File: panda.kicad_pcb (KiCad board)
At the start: 2 copper layers, 100 x 125 mm, 196 parts, among them J1 PIN10-13_Breakout, J10 24V_Lockout_Key_Switch, J11 XT60-M, J12 PT_1, J13 PT_4, J14 PT_2, J15 PT_5, J16 PT_3, J17 PT_6, J18 4-Pin Load Cell, J19 5-Pin Load Cell, J2 PIN6-9_Breakout, J20 Ignitor Screw Terminal, J21 Screw_Terminal_01x03, J22 Screw_Terminal_01x02, J3 USB_C_Receptacle_USB2.0_16P, J4 Valve_1_PWR, J5 Valve_4_PWR, J6 Valve_2_PWR, J7 Valve_5_PWR, J8 Valve_3_PWR, J9 Valve_6_PWR, K1 G5Q-1A DC24, K2 G5Q-1A DC24, Q1 BSS138, Q2 BSS138, Q3 BSS138, Q4 BSS138, Q5 BSS138, Q6 BSS138, Q7 BSS138, Q8 BSS138, SW1 PTS636SM43SMTR LFS, SW2 PTS636SM43SMTR LFS, U1 ESP32-S3-WROOM-1, U2 ADS112C04, U3 ADS112C04, U4 ADS112C04, U5 ADS112C04, U6 TPS5430DDA, U7 XC6220B331PR-G, U8 INA199A2DCK

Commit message: pcb first draft, changed esp32 pin connections
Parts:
- removed the C15 at (263.8, 51.6)
- removed the C15 at (249.8, 59.5)
- removed the C5 at (205.4, 99.3)
- removed the C5 at (211.0, 71.5)
- removed J2: PIN6-9_Breakout, TerminalBlock:TerminalBlock_Xinya_XY308-2.54-4P_1x04_P2.54mm_Horizontal
- removed the R2 at (202.0, 90.8)
- added C15: 10uF, Capacitor_SMD:C_1206_3216Metric, F.Cu at (122.2, 70.7)
- added C22: 0.1uF, Capacitor_SMD:C_0603_1608Metric, F.Cu at (131.1, 36.6)
- added C23: 0.1uF, Capacitor_SMD:C_0603_1608Metric, F.Cu at (131.1, 30.0)
- added C5: 0.1uF, Capacitor_SMD:C_0402_1005Metric, F.Cu at (153.1, 36.1)
- added D17: TSD24DYFR, Diode_SMD:D_SOD-323, F.Cu at (129.3, 36.6)
- added D18: TSD24DYFR, Diode_SMD:D_SOD-323, F.Cu at (129.3, 29.9)
- added R47: 10, Resistor_SMD:R_0402_1005Metric, F.Cu at (127.5, 34.3)
- added R48: 10, Resistor_SMD:R_0402_1005Metric, F.Cu at (127.5, 32.0)
- moved C19 164.5 mm to (119.0, 82.4)
- moved D12 152.4 mm to (118.2, 69.4)
- moved R37 150.1 mm to (130.1, 61.3), turned to 90 degrees
- moved D13 149.0 mm to (122.2, 68.2), turned to 0 degrees
- moved U7 140.4 mm to (120.2, 75.5), turned to -90 degrees
- moved C17 133.8 mm to (120.0, 80.4)
- moved D15 127.3 mm to (127.7, 61.3)
- moved R36 113.0 mm to (125.2, 68.2), turned to -90 degrees
- moved TP4 112.8 mm to (117.2, 84.2), turned to 180 degrees
- moved G*** 94.1 mm to (134.4, 95.1)
- moved R7 84.1 mm to (155.7, 64.5)
- moved R8 84.0 mm to (155.7, 65.8)
- moved C2 79.6 mm to (156.5, 57.7), turned to 180 degrees
- moved J1 77.9 mm to (165.4, 105.7)
- moved D8 76.0 mm to (127.7, 52.5)
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- renumbered C22 to C24, C23 to C25, C24 to C26, C25 to C27, C26 to C28, C27 to C29, C28 to C30, C29 to C31, C30 to C32, C31 to C33, C32 to C34, C33 to C35, C34 to C36, C35 to C37, C36 to C38, C37 to C39, D8 to D10, D10 to D11, D11 to D12, D12 to D13, D13 to D14, D14 to D15, D15 to D16, D16 to D19, D17 to D20, D18 to D21, D19 to D22, D20 to D23, D21 to D24, D22 to D25, D23 to D26, D24 to D27, D25 to D28, D26 to D29, D27 to D30, D28 to D31, D29 to D32, D30 to D33, D31 to D34, D32 to D35, D33 to D36, D34 to D8, J11 to J10, J10 to J11, R11 to R10, R12 to R11, R13 to R12, R14 to R13, R15 to R14, R16 to R15, R17 to R16, R18 to R17, R19 to R18, R20 to R19, R3 to R2, R21 to R20, R22 to R21, R23 to R22, R24 to R23, R25 to R24, R26 to R25, R27 to R26, R28 to R27, R29 to R28, R68 to R29, R4 to R3, R33 to R32, R32 to R33, R5 to R4, R47 to R49, R6 to R5, R48 to R50, R49 to R51, R50 to R52, R51 to R53, R52 to R54, R53 to R55, R54 to R56, R55 to R57, R56 to R58, R57 to R59, R7 to R6, R58 to R60, R59 to R61, R60 to R62, R61 to R63, R62 to R64, R63 to R65, R64 to R66, R65 to R67, R66 to R68, R67 to R69, R8 to R7, R9 to R8, R10 to R9
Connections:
- F1 pad 2: Net-(U8-+) -> Net-(F1-Pad2)
- J1 pad 1: unconnected-(J1-Pin_1-Pad1) -> MTMS
- J1 pad 2: unconnected-(J1-Pin_2-Pad2) -> MTDI
- J1 pad 3: unconnected-(J1-Pin_3-Pad3) -> MTDO
- J1 pad 4: unconnected-(J1-Pin_4-Pad4) -> MTCK
- J3 pad S1: Net-(J3-SHIELD) -> unconnected-(J3-SHIELD-PadS1)
- R49 pad 1: Net-(U8-+) -> Net-(F1-Pad2)
- U1 pad 10: VALVE_4_CTL -> VALVE_5_CTL
- U1 pad 11: VALVE_5_CTL -> VALVE_4_CTL
- U1 pad 12: VALVE_6_CTL -> VALVE_3_CTL
- U1 pad 15: I2C_SCL -> I2C_SDA
- U1 pad 16: I2C_SDA -> I2C_SCL
- U1 pad 32: unconnected-(U1-IO39-Pad32) -> MTCK
- U1 pad 33: unconnected-(U1-IO40-Pad33) -> MTDO
- U1 pad 34: unconnected-(U1-IO41-Pad34) -> MTDI
- U1 pad 35: unconnected-(U1-IO42-Pad35) -> MTMS
- U1 pad 4: IGNITOR_CTL -> SAFE_24V_CTL
- U1 pad 5: SAFE_24V_CTL -> IGNITOR_CTL
- U1 pad 7: VALVE_2_CTL -> VALVE_1_CTL
- U1 pad 8: VALVE_1_CTL -> VALVE_2_CTL
- U1 pad 9: VALVE_3_CTL -> VALVE_6_CTL
- U8 pad 4: Net-(U8-+) -> Net-(D17-K)
- U8 pad 5: /Ignitor Control/IGNITOR_+VE -> Net-(D18-K)
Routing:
- net VALVE_3_CTL: track 24.9 -> 104.3 mm, vias 0 -> 2
- net +3.3V: track 179.6 -> 254.8 mm, vias 6 -> 12
- net I2C_DRDY_ADC1: track 23.6 -> 95.6 mm
- net VALVE_1_CTL: track 19.2 -> 89.9 mm, vias 0 -> 2
- net 5V_USB: track 7.01 -> 74.8 mm, vias 0 -> 3
- net VALVE_2_CTL: track 32.3 -> 98.8 mm, vias 0 -> 2
- net VALVE_4_CTL: track 34.8 -> 97.0 mm, vias 0 -> 2
- net BOOT: track 0.00 -> 49.4 mm, vias 0 -> 2
- net I2C_DRDY_ADC2: track 34.4 -> 81.1 mm
- net VALVE_5_CTL: track 45.9 -> 89.7 mm, vias 0 -> 2
- net /Power Regulation/+24V_POST_LOCKOUT: track 30.3 -> 72.5 mm, vias 0 -> 1
- net SAFE_24V_CTL: track 33.1 -> 72.7 mm, vias 1 -> 2
- net USB_P: track 0.00 -> 39.6 mm
- net USB_N: track 0.00 -> 35.3 mm
- net MTCK: track 0.00 -> 34.2 mm
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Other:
- board text added: "+3.3V"
- board text added: "BOOT"
- board text added: "KEY+24V"
- board text added: "RST"
- board text added: "https://github.com/Queens-Rocket-Engineering-Team/prop-pandaV2"
- board text removed: "https://github.com/Queens-Rocket-Engineering-Team/prop-panda"

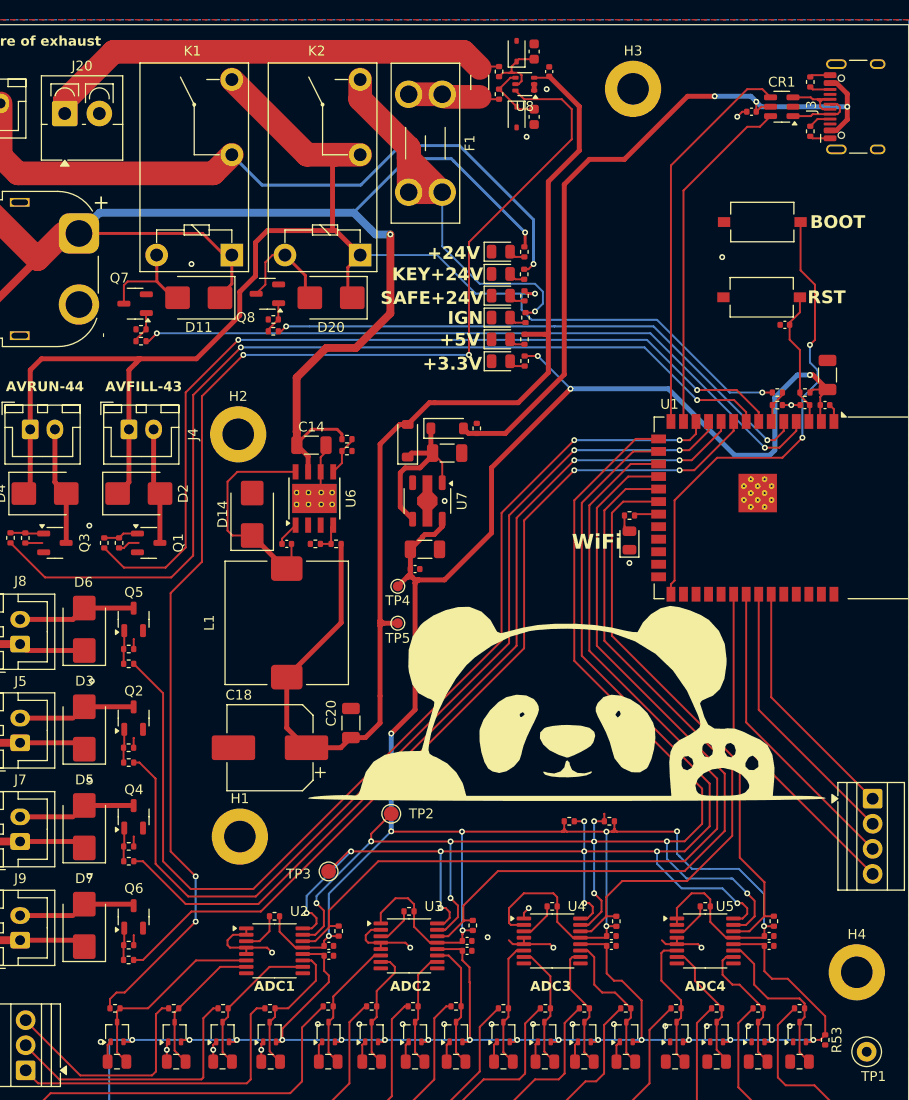
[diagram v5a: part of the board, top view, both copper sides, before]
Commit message: replaced ignitor current sensor with INA187A3 for higher voltage tolerance
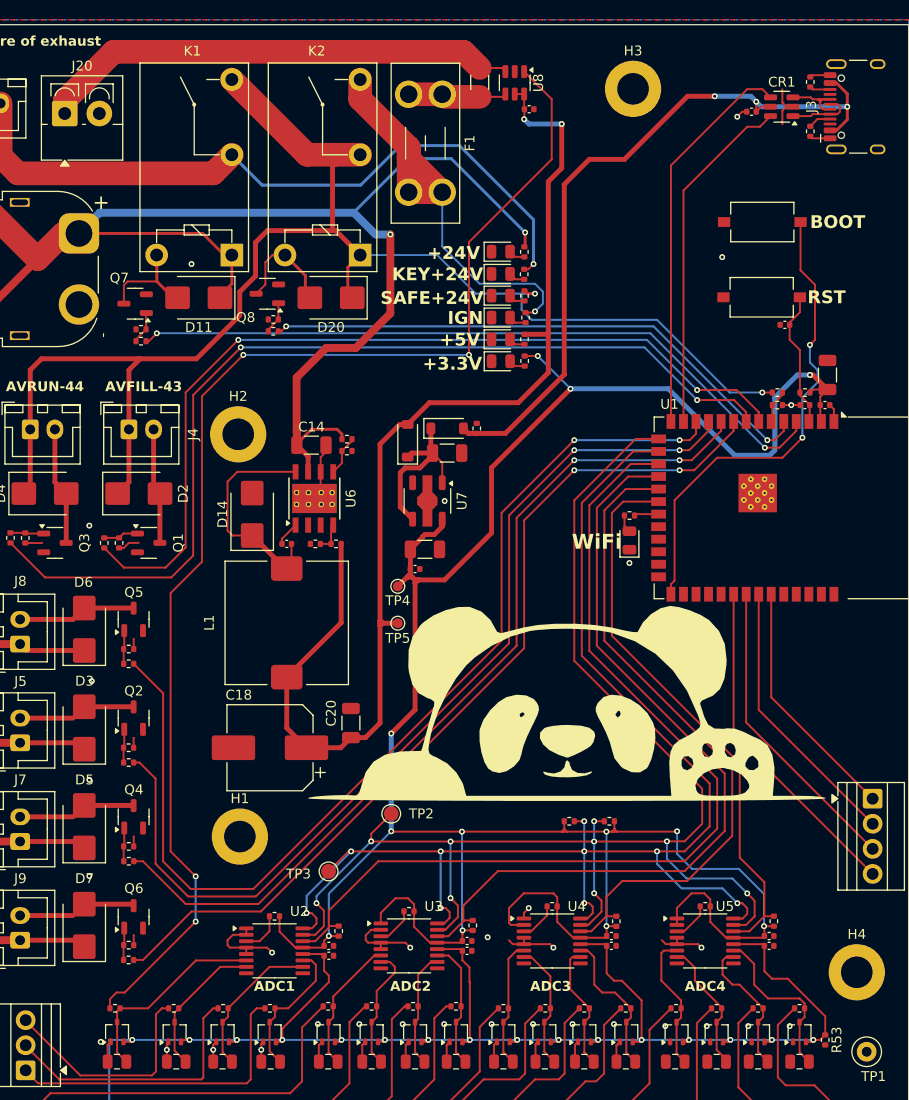
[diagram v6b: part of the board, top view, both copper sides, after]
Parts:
- removed C22, C23: 0.1uF, Capacitor_SMD:C_0603_1608Metric
- removed D17, D18: TSD24DYFR, Diode_SMD:D_SOD-323
- removed R47, R48: 10, Resistor_SMD:R_0402_1005Metric
- U8: value INA199A2DCK -> INA187A3; footprint Package_TO_SOT_SMD:SOT-363_SC-70-6 -> Package_TO_SOT_SMD:SOT-23-6
- moved C21 4.32 mm to (130.6, 35.8), turned to 180 degrees
- moved U8 1.02 mm to (129.1, 33.1), turned to -90 degrees
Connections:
- F1 pad 2: Net-(F1-Pad2) -> Net-(U8--)
- R49 pad 1: Net-(F1-Pad2) -> Net-(U8--)
- U8 pad 1: GND -> IGN_Current_Measurement
- U8 pad 3: +5V -> /Ignitor Control/IGNITOR_+VE
- U8 pad 4: Net-(D17-K) -> Net-(U8--)
- U8 pad 5: Net-(D18-K) -> +5V
- U8 pad 6: IGN_Current_Measurement -> +5V
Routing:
- net Net-(F1-Pad2): track 10.5 -> 0.00 mm
- net Net-(U8--): track 0.00 -> 10.0 mm
- net Net-(D18-K): track 7.74 -> 0.00 mm
- net Net-(D17-K): track 6.53 -> 0.00 mm
- net +24V: track 427.4 -> 423.2 mm
- net GND: track 77.0 -> 80.9 mm, vias 40 -> 38
- net IGN_Current_Measurement: track 132.9 -> 130.6 mm
- net +5V: track 289.8 -> 288.6 mm, vias 16 -> 18
- net +3.3V: track 254.8 -> 253.8 mm
- net I2C_SDA: track 141.9 -> 141.1 mm
- net /Ignitor Control/IGNITOR_+VE: track 49.5 -> 48.8 mm
- net BOOT: track 49.4 -> 48.9 mm

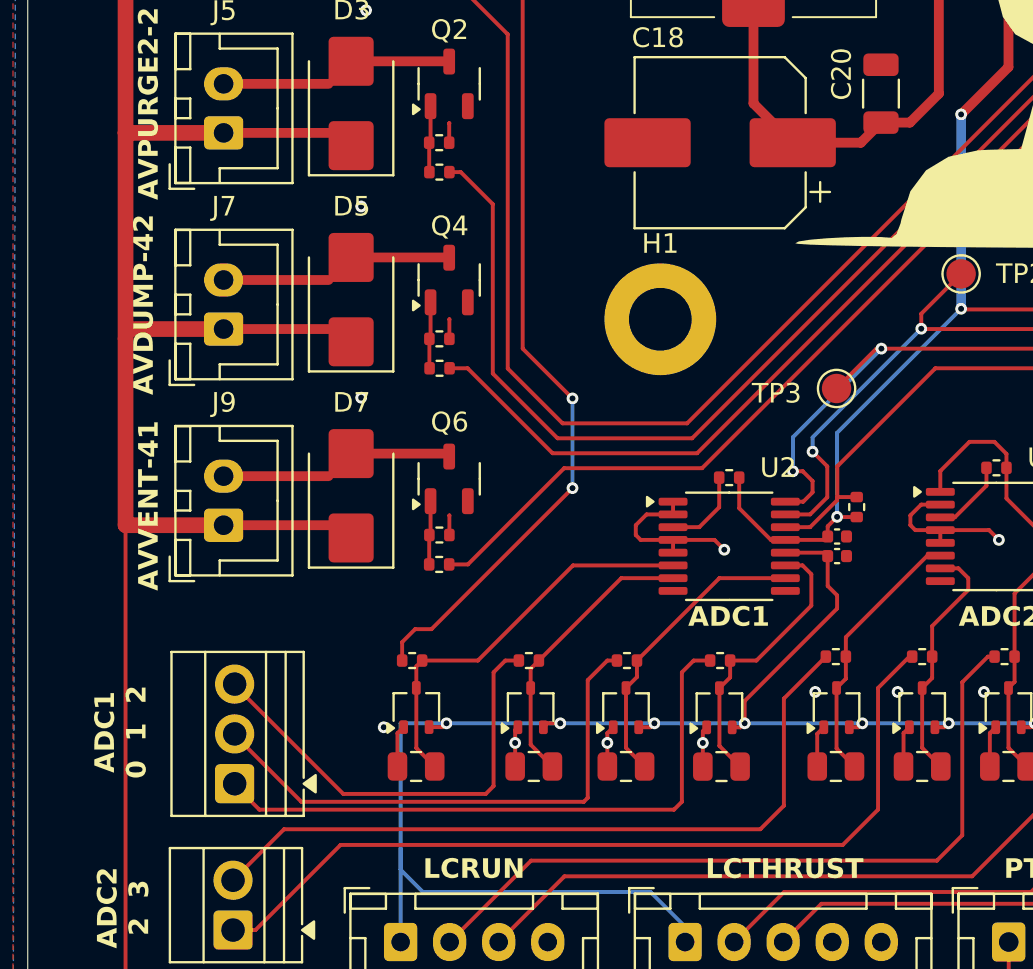
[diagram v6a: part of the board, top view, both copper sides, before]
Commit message: fixed 5v rail connection for signal conditioning
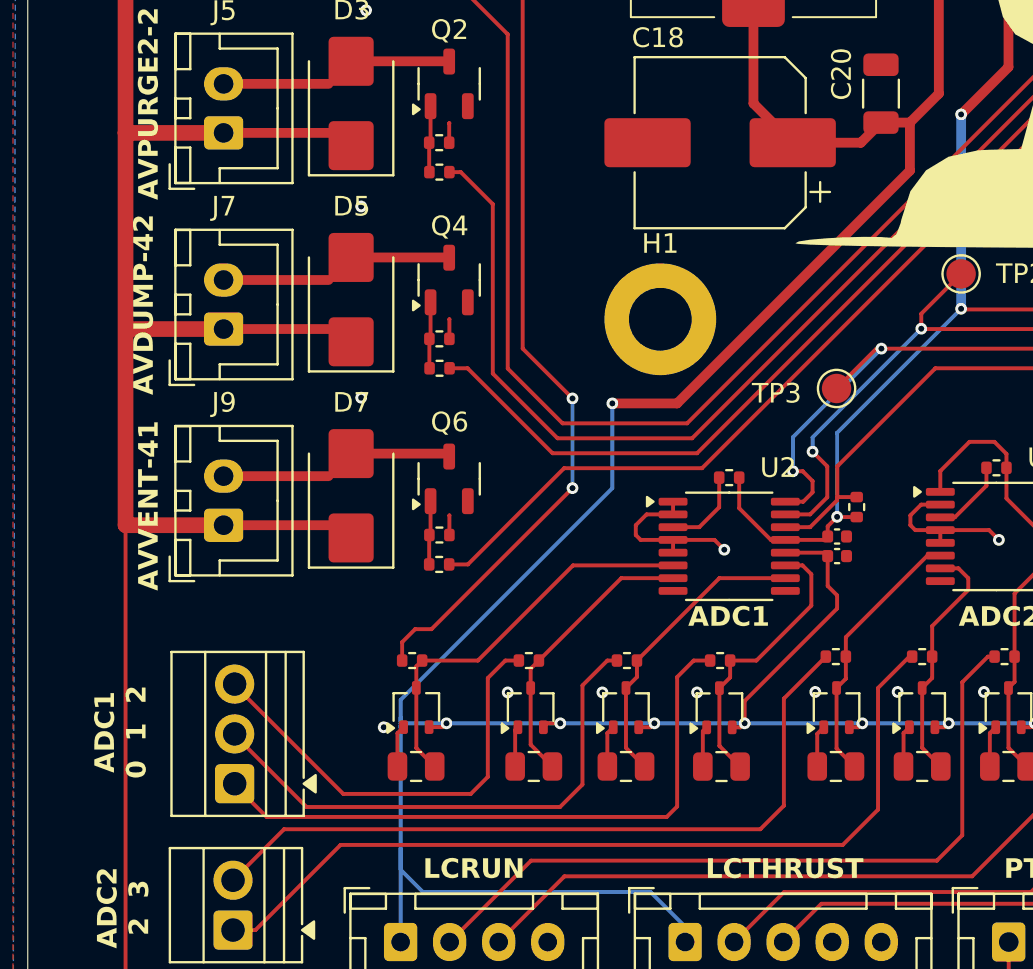
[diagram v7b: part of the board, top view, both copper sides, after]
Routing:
- net +5V: track 288.6 -> 332.5 mm, vias 18 -> 19
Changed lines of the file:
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@@
 	)
 	(segment
-		(start 93.85 132.3)
-		(end 93.85 131.1)
-		(width 0.2)
-		(layer "F.Cu")
-		(net 2)
-	)
-	(segment
 		(start 130.025 120.4)
 		(end 128.9 120.4)
@@
 	)
 	(segment
-		(start 103.418783 131.1)
+		(start 103.418783 132.305779)
 		(end 103.418783 130.500779)
 		(width 0.2)
@@
 	)
 	(segment
-		(start 93.85 131.1)
+		(start 93.85 132.3)
 		(end 93.85 130.44)
 		(width 0.2)
@@
 	)
 	(segment
-		(start 98.55 131.1)
-		(end 98.55 130.6)
-		(width 0.2)
-		(layer "F.Cu")
-		(net 2)
-	)
-	(segment
 		(start 98.55 132.3)
-		(end 98.55 131.1)
+		(end 98.55 130.6)
 		(width 0.2)
 		(layer "F.Cu")
@@
 	)
 	(segment
-		(start 103.418783 132.305779)
-		(end 103.418783 131.1)
-		(width 0.2)
-		(layer "F.Cu")
-		(net 2)
-	)
-	(segment
 		(start 157.287 35.562)
 		(end 156.624501 35.562)
@@
 	)
 	(via
-		(at 96.35 51.5)
+		(at 98.298 128.524)
 		(size 0.6)
 		(drill 0.3)
@@
 	)
 	(via
-		(at 109.15 128.5)
+		(at 96.35 51.5)
 		(size 0.6)
 		(drill 0.3)
@@
 	)
 	(via
-		(at 93.85 131.1)
+		(at 109.15 128.5)
 		(size 0.6)
 		(drill 0.3)
 		(layers "F.Cu" "B.Cu")
+		(free yes)
 		(net 2)
 	)
@@
 	)
 	(via
-		(at 103.418783 131.1)
+		(at 118.512501 120.75)
 		(size 0.6)
 		(drill 0.3)
 		(layers "F.Cu" "B.Cu")
+		(free yes)
 		(net 2)
 	)
 	(via
-		(at 118.512501 120.75)
+		(at 104.512501 121.25)
 		(size 0.6)
 		(drill 0.3)
@@
 	)
 	(via
-		(at 104.512501 121.25)
+		(at 103.124 128.524)
 		(size 0.6)
 		(drill 0.3)
@@
 	)
 	(via
+		(at 93.472 128.524)
+		(size 0.6)
+		(drill 0.3)
+		(layers "F.Cu" "B.Cu")
+		(free yes)
+		(net 2)
+	)
+	(via
 		(at 141.012501 139.75)
 		(size 0.6)
@@
 	)
 	(via
-		(at 98.55 131.1)
-		(size 0.6)
-		(drill 0.3)
-		(layers "F.Cu" "B.Cu")
-		(net 2)
-	)
-	(via
 		(at 86 78)
 		(size 0.6)
@@
 	)
 	(segment
+		(start 102.108 113.792)
+		(end 98.806 113.792)
+		(width 0.5)
+		(layer "F.Cu")
+		(net 3)
+	)
+	(segment
 		(start 107.624999 121.4)
 		(end 109.607499 121.4)
@@
 	)
 	(segment
+		(start 113.975 101.925)
+		(end 102.108 113.792)
+		(width 0.5)
+		(layer "F.Cu")
+		(net 3)
+	)
+	(segment
 		(start 124.35 130.3)
 		(end 124.55 130.1)
@@
 	)
 	(segment
+		(start 113.975 99.475)
+		(end 113.975 101.925)
+		(width 0.5)
+		(layer "F.Cu")
+		(net 3)
+	)
+	(segment
 		(start 89.461924 130.292887)
 		(end 90.157113 130.292887)
@@
 	)
 	(via
+		(at 98.806 113.792)
+		(size 0.6)
+		(drill 0.3)
+		(layers "F.Cu" "B.Cu")
+		(net 3)
+	)
+	(via
 		(at 146.75 130.1)
 		(size 0.6)
@@
 	)
 	(segment
+		(start 88.012501 130.1)
+		(end 88.012501 129.794)
+		(width 0.2)
+		(layer "B.Cu")
+		(net 3)
+	)
+	(segment
 		(start 105.55 130.1)
 		(end 111.55 130.1)
@@
 	)
 	(segment
+		(start 88.012501 130.302)
+		(end 88.012501 130.225499)
+		(width 0.2)
+		(layer "B.Cu")
+		(net 3)
+	)
+	(segment
 		(start 137.55 130.1)
 		(end 141.95 130.1)
@@
 	)
 	(segment
+		(start 88.012501 129.794)
+		(end 88.012501 129.974501)
+		(width 0.2)
+		(layer "B.Cu")
+		(net 3)
+	)
+	(segment
+		(start 98.806 113.792)
+		(end 98.806 118.11)
+		(width 0.2)
+		(layer "B.Cu")
+		(net 3)
+	)
+	(segment
 		(start 88.012501 136.5)
 		(end 88.012501 141.25)
@@
 	)
 	(segment
+		(start 88.012501 130.1)
+		(end 88.138 130.1)
+		(width 0.2)
+		(layer "B.Cu")
+		(net 3)
+	)
+	(segment
+		(start 88.012501 128.903499)
+		(end 88.012501 129.794)
+		(width 0.2)
+		(layer "B.Cu")
+		(net 3)
+	)
+	(segment
+		(start 98.806 118.11)
+		(end 88.012501 128.903499)
+		(width 0.2)
+		(layer "B.Cu")
+		(net 3)
+	)
+	(segment
 		(start 102.512501 141.25)
 		(end 102.512501 140.462501)
@@
 	)
 	(segment
-		(start 88.012501 130.1)
+		(start 88.138 130.1)
 		(end 90.35 130.1)
 		(width 0.2)
@@
 	)
 	(segment
+		(start 88.012501 130.225499)
+		(end 88.138 130.1)
+		(width 0.2)
+		(layer "B.Cu")
+		(net 3)
+	)
+	(segment
 		(start 129.35 130.1)
 		(end 133.55 130.1)
@@
 	(segment
 		(start 88.012501 130.1)
-		(end 88.012501 136.5)
+		(end 88.012501 130.302)
 		(width 0.2)
 		(layer "B.Cu")
@@
 	)
 	(segment
+		(start 88.012501 130.302)
+		(end 88.012501 136.5)
+		(width 0.2)
+		(layer "B.Cu")
+		(net 3)
+	)
+	(segment
 		(start 133.858 37.31)
 		(end 130.528 37.31)
@@
 	)
 	(segment
+		(start 88.012501 129.974501)
+		(end 88.138 130.1)
+		(width 0.2)
+		(layer "B.Cu")
+		(net 3)
+	)
+	(segment
 		(start 155.15 130.1)
 		(end 159.35 130.1)
@@
 	)
 	(segment
-		(start 73.987501 110.5)
+		(start 73.987501 120)
 		(end 73.987501 100)
 		(width 0.8)
@@
 	)
 	(segment
-		(start 73.987501 120)
-		(end 73.987501 110.5)
-		(width 0.8)
-		(layer "F.Cu")
-		(net 4)
-	)
-	(segment
 		(start 85.487501 90.65)
 		(end 79.637501 90.65)
@@
 	)
 	(segment
-		(start 82.951 134.101)
-		(end 97.349 134.101)
+		(start 98.55 126.9)
+		(end 99.04 126.9)
 		(width 0.2)
 		(layer "F.Cu")
@@
 	)
 	(segment
-		(start 97.55 133.9)
-		(end 97.55 127.9)
+		(start 83.216 134.366)
+		(end 96.139 134.366)
 		(width 0.2)
 		(layer "F.Cu")
@@
 	)
 	(segment
-		(start 97.55 127.9)
-		(end 98.55 126.9)
+		(start 97.282 133.223)
+		(end 97.282 128.168)
 		(width 0.2)
 		(layer "F.Cu")
@@
 	)
 	(segment
-		(start 79.55 130.7)
-		(end 82.951 134.101)
+		(start 97.282 128.168)
+		(end 98.55 126.9)
 		(width 0.2)
 		(layer "F.Cu")
@@
 	)
 	(segment
-		(start 98.55 126.9)
-		(end 99.04 126.9)
+		(start 79.55 130.7)
+		(end 83.216 134.366)
 		(width 0.2)
 		(layer "F.Cu")
@@
 	)
 	(segment
-		(start 97.349 134.101)
-		(end 97.55 133.9)
+		(start 96.139 134.366)
+		(end 97.282 133.223)
 		(width 0.2)
 		(layer "F.Cu")
@@
 	)
 	(segment
-		(start 102.95 126.9)
-		(end 103.79 126.9)
+		(start 79.55 133.24)
+		(end 81.184 134.874)
 		(width 0.2)
 		(layer "F.Cu")
@@
 	)
 	(segment
-		(start 80.812 134.502)
-		(end 101.948 134.502)
+		(start 81.184 134.874)
+		(end 101.576 134.874)
 		(width 0.2)
 		(layer "F.Cu")
@@
 	)
 	(segment
-		(start 102.35 134.1)
-		(end 102.35 127.5)
+		(start 102.108 127.742)
+		(end 102.95 126.9)
 		(width 0.2)
 		(layer "F.Cu")
@@
 	)
 	(segment
-		(start 101.948 134.502)
-		(end 102.35 134.1)
+		(start 102.108 134.342)
+		(end 102.108 127.742)
 		(width 0.2)
 		(layer "F.Cu")
@@
 	)
 	(segment
-		(start 79.55 133.24)
-		(end 80.812 134.502)
+		(start 102.95 126.9)
+		(end 103.79 126.9)
 		(width 0.2)
 		(layer "F.Cu")
@@
 	)
 	(segment
-		(start 102.35 127.5)
-		(end 102.95 126.9)
+		(start 101.576 134.874)
+		(end 102.108 134.342)
 		(width 0.2)
 		(layer "F.Cu")
@@
 	)
 	(segment
-		(start 92.75 127.5)
-		(end 93.35 126.9)
+		(start 92.456 132.832)
+		(end 92.456 127.794)
 		(width 0.2)
 		(layer "F.Cu")
@@
 	)
 	(segment
-		(start 92.35 133.7)
-		(end 92.75 133.3)
+		(start 79.55 128.16)
+		(end 85.09 133.7)
 		(width 0.2)
 		(layer "F.Cu")
@@
 	)
 	(segment
-		(start 85.09 133.7)
-		(end 92.35 133.7)
+		(start 91.588 133.7)
+		(end 92.456 132.832)
 		(width 0.2)
 		(layer "F.Cu")
@@
 	)
 	(segment
-		(start 79.55 128.16)
-		(end 85.09 133.7)
+		(start 92.456 127.794)
+		(end 93.35 126.9)
 		(width 0.2)
 		(layer "F.Cu")
@@
 	)
 	(segment
-		(start 92.75 133.3)
-		(end 92.75 127.5)
+		(start 85.09 133.7)
+		(end 91.588 133.7)
 		(width 0.2)
 		(layer "F.Cu")
